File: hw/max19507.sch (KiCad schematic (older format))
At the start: 51 parts, among them U10 LMH6882, U8 THS4522, U9 MAX19507

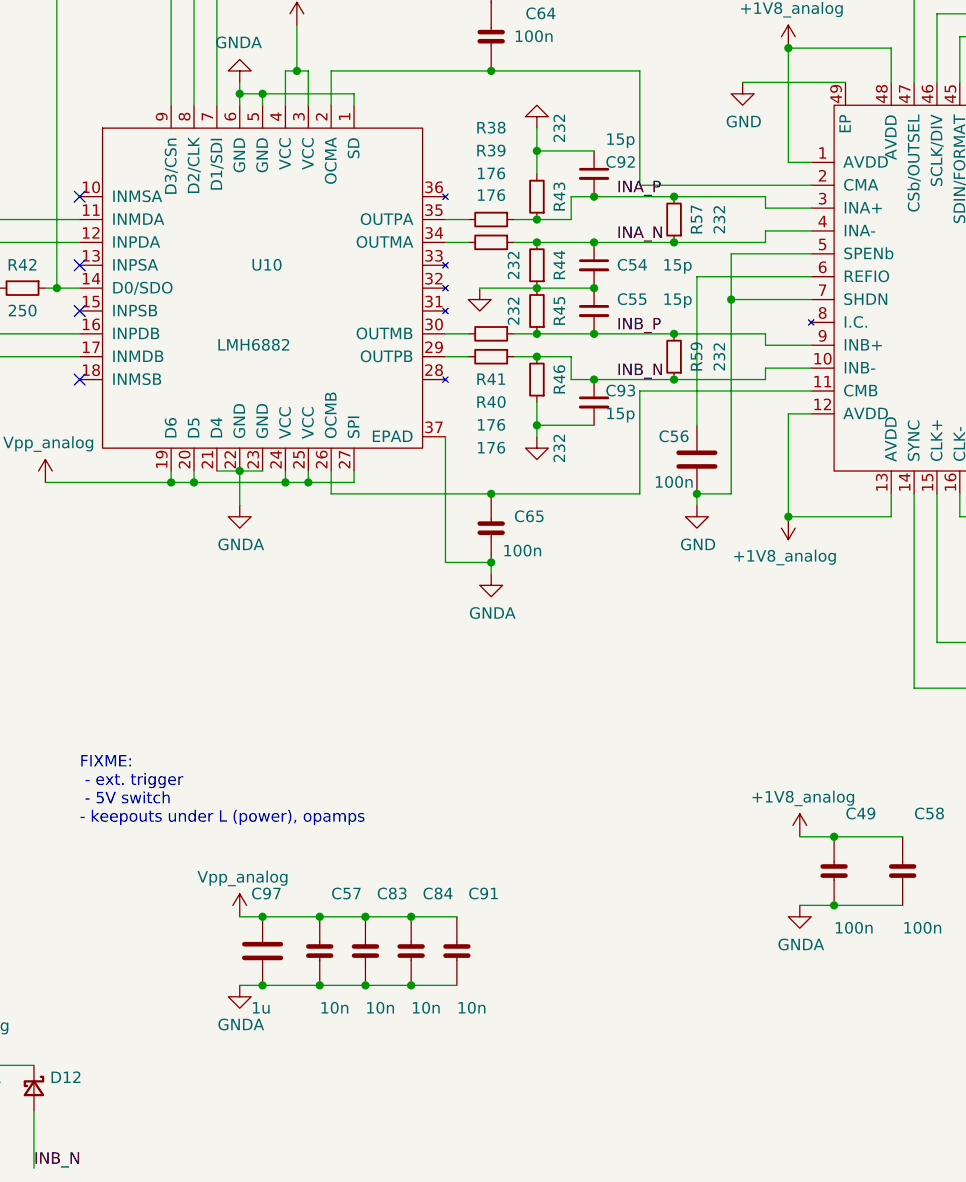
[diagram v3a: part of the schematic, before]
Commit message: everything hooked up + layed out; 0.2/0.4mm vias :-(
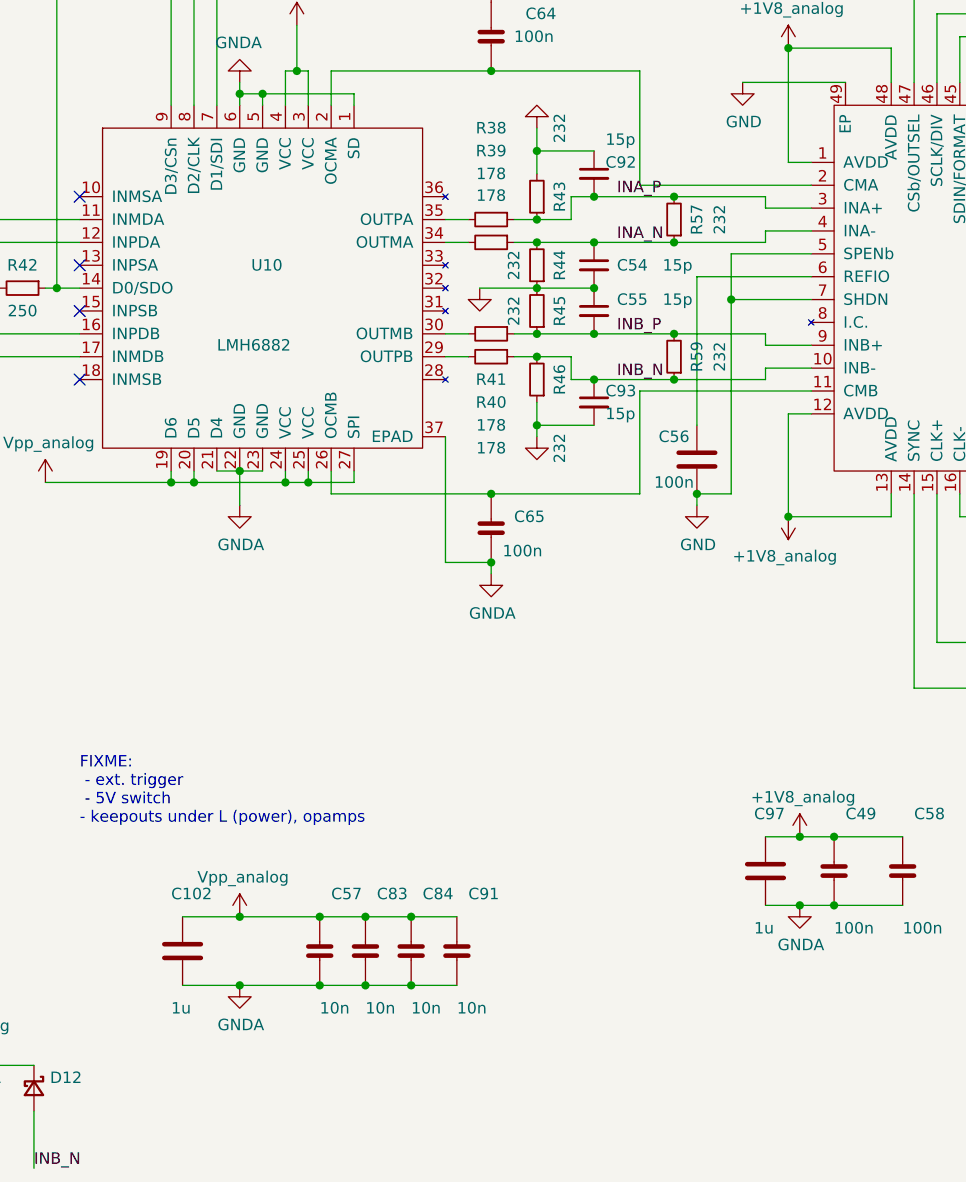
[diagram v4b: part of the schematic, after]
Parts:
- added C102: 1u, Capacitor_SMD:C_0805_2012Metric, symbol fmc:1uF_805
- R38, R39, R40, R41: value 176 -> 178
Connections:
- net +1V8_analog: now also C97.1
- net GNDA: now also C102.2
- net Vpp_analog: now also C102.1; no longer C97.1
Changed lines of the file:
@@
 $Descr A4 11693 8268
 encoding utf-8
-Sheet 5 8
+Sheet 6 9
 Title ""
 Date ""
@@
 P 6550 3100
 F 0 "R38" V 6150 3100 50  0000 C CNN
-F 1 "176" V 6445 3100 50  0000 C CNN
+F 1 "178" V 6445 3100 50  0000 C CNN
 F 2 "Resistor_SMD:R_0603_1608Metric" H 6550 3100 50  0001 C CNN
 F 3 "~" H 6550 3100 50  0001 C CNN
@@
 P 6550 3200
 F 0 "R39" V 6150 3200 50  0000 C CNN
-F 1 "176" V 6250 3200 50  0000 C CNN
+F 1 "178" V 6250 3200 50  0000 C CNN
 F 2 "Resistor_SMD:R_0603_1608Metric" H 6550 3200 50  0001 C CNN
 F 3 "~" H 6550 3200 50  0001 C CNN
@@
 P 6550 3600
 F 0 "R40" V 6850 3600 50  0000 C CNN
-F 1 "176" V 7050 3600 50  0000 C CNN
+F 1 "178" V 7050 3600 50  0000 C CNN
 F 2 "Resistor_SMD:R_0603_1608Metric" H 6550 3600 50  0001 C CNN
 F 3 "~" H 6550 3600 50  0001 C CNN
@@
 P 6550 3700
 F 0 "R41" V 6650 3700 50  0000 C CNN
-F 1 "176" V 6850 3700 50  0000 C CNN
+F 1 "178" V 6850 3700 50  0000 C CNN
 F 2 "Resistor_SMD:R_0603_1608Metric" H 6550 3700 50  0001 C CNN
 F 3 "~" H 6550 3700 50  0001 C CNN
@@
 	1    0    0    -1
 $EndComp
-Wire Wire Line
-	5450 6150 5550 6150
 Connection ~ 5800 6150
 Wire Wire Line
@@
 	4050 5950 3750 5950
 Connection ~ 3750 5950
-$Comp
-L fmc:1uF_805 C?
-U 1 1 60DB1CC7
-P 5550 6300
-AR Path="/60B16D71/60DB1CC7" Ref="C?"  Part="1"
-AR Path="/612B1274/60DB1CC7" Ref="C97"  Part="1"
-F 0 "C97" H 5500 6550 50  0000 L CNN
-F 1 "1u" H 5500 6050 50  0000 L CNN
-F 2 "Capacitor_SMD:C_0805_2012Metric" H 5588 6150 50  0001 C CNN
-F 3 "~" H 5550 6300 50  0001 C CNN
-F 4 "GCJ219R71C105KA01" H 5675 6500 50  0001 C CNN "Part"
-F 5 "Murata" H 5775 6600 50  0001 C CNN "Manufacturer"
-	1    5550 6300
-	1    0    0    -1
-$EndComp
-Wire Wire Line
-	5550 6450 5450 6450
-Wire Wire Line
-	5550 6150 5800 6150
-Connection ~ 5550 6150
-Wire Wire Line
-	5550 6450 5800 6450
-Connection ~ 5550 6450
 Wire Wire Line
 	4750 3600 4350 3600
@@
 	6350 4600 6350 4050
 Connection ~ 6550 4600
+$Comp
+L fmc:1uF_805 C?
+U 1 1 60E328FC
+P 5200 6300
+AR Path="/60B16D71/60E328FC" Ref="C?"  Part="1"
+AR Path="/612B1274/60E328FC" Ref="C102"  Part="1"
+F 0 "C102" H 5150 6550 50  0000 L CNN
+F 1 "1u" H 5150 6050 50  0000 L CNN
+F 2 "Capacitor_SMD:C_0805_2012Metric" H 5238 6150 50  0001 C CNN
+F 3 "~" H 5200 6300 50  0001 C CNN
+F 4 "GCJ219R71C105KA01" H 5325 6500 50  0001 C CNN "Part"
+F 5 "Murata" H 5425 6600 50  0001 C CNN "Manufacturer"
+	1    5200 6300
+	1    0    0    -1
+$EndComp
+Wire Wire Line
+	5200 6150 5450 6150
+Connection ~ 5450 6150
+Wire Wire Line
+	5200 6450 5450 6450
+Connection ~ 5450 6450
+$Comp
+L fmc:1uF_805 C?
+U 1 1 60E69665
+P 7750 5950
+AR Path="/60B16D71/60E69665" Ref="C?"  Part="1"
+AR Path="/612B1274/60E69665" Ref="C97"  Part="1"
+F 0 "C97" H 7700 6200 50  0000 L CNN
+F 1 "1u" H 7700 5700 50  0000 L CNN
+F 2 "Capacitor_SMD:C_0805_2012Metric" H 7788 5800 50  0001 C CNN
+F 3 "~" H 7750 5950 50  0001 C CNN
+F 4 "GCJ219R71C105KA01" H 7875 6150 50  0001 C CNN "Part"
+F 5 "Murata" H 7975 6250 50  0001 C CNN "Manufacturer"
+	1    7750 5950
+	1    0    0    -1
+$EndComp
+Wire Wire Line
+	7750 5800 7900 5800
+Connection ~ 7900 5800
+Wire Wire Line
+	7750 6100 7900 6100
+Connection ~ 7900 6100
+Wire Wire Line
+	5450 6150 5800 6150
+Wire Wire Line
+	5450 6450 5800 6450
 $EndSCHEMATC

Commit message: prototype version
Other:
- note added: "FIXME: -*-"
- note removed: "FIXME:\n - ext. trigger\n - 5V switch\n- keepouts under L (power), opamps"
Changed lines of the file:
@@
 F2 "OUT" I R 1900 4050 50
 $EndSheet
-Text Notes 4750 5750 0    50   ~ 0
-FIXME:\n - ext. trigger\n - 5V switch\n- keepouts under L (power), opamps
+Text Notes 4750 5050 0    50   ~ 0
+FIXME: -*-
 Wire Wire Line
 	2250 2300 2450 2300
